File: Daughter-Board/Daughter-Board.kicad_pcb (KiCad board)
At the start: 2 copper layers, 79 parts, among them J201 302-S101, J301 Conn_01x08_0.5mm_Female_Kyoce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, J401 Conn_01x08_0.5mm_Female_Kyoce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, J501 Conn_01x08_0.5mm_Female_Kyoce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, J601 Conn_01x08_0.5mm_Female_Kyoce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, P101 EdgeConn, P102 EdgeConn, U101 LMV934MA, U102 MC74VHCT126A, U103 MC74VHCT126A, U104 4016, U105 4016, U106 4016, U107 4016, U108 4016, U201 74HC540, U202 PIC32MZ2048EFM064-TQFP, U301 LM324A

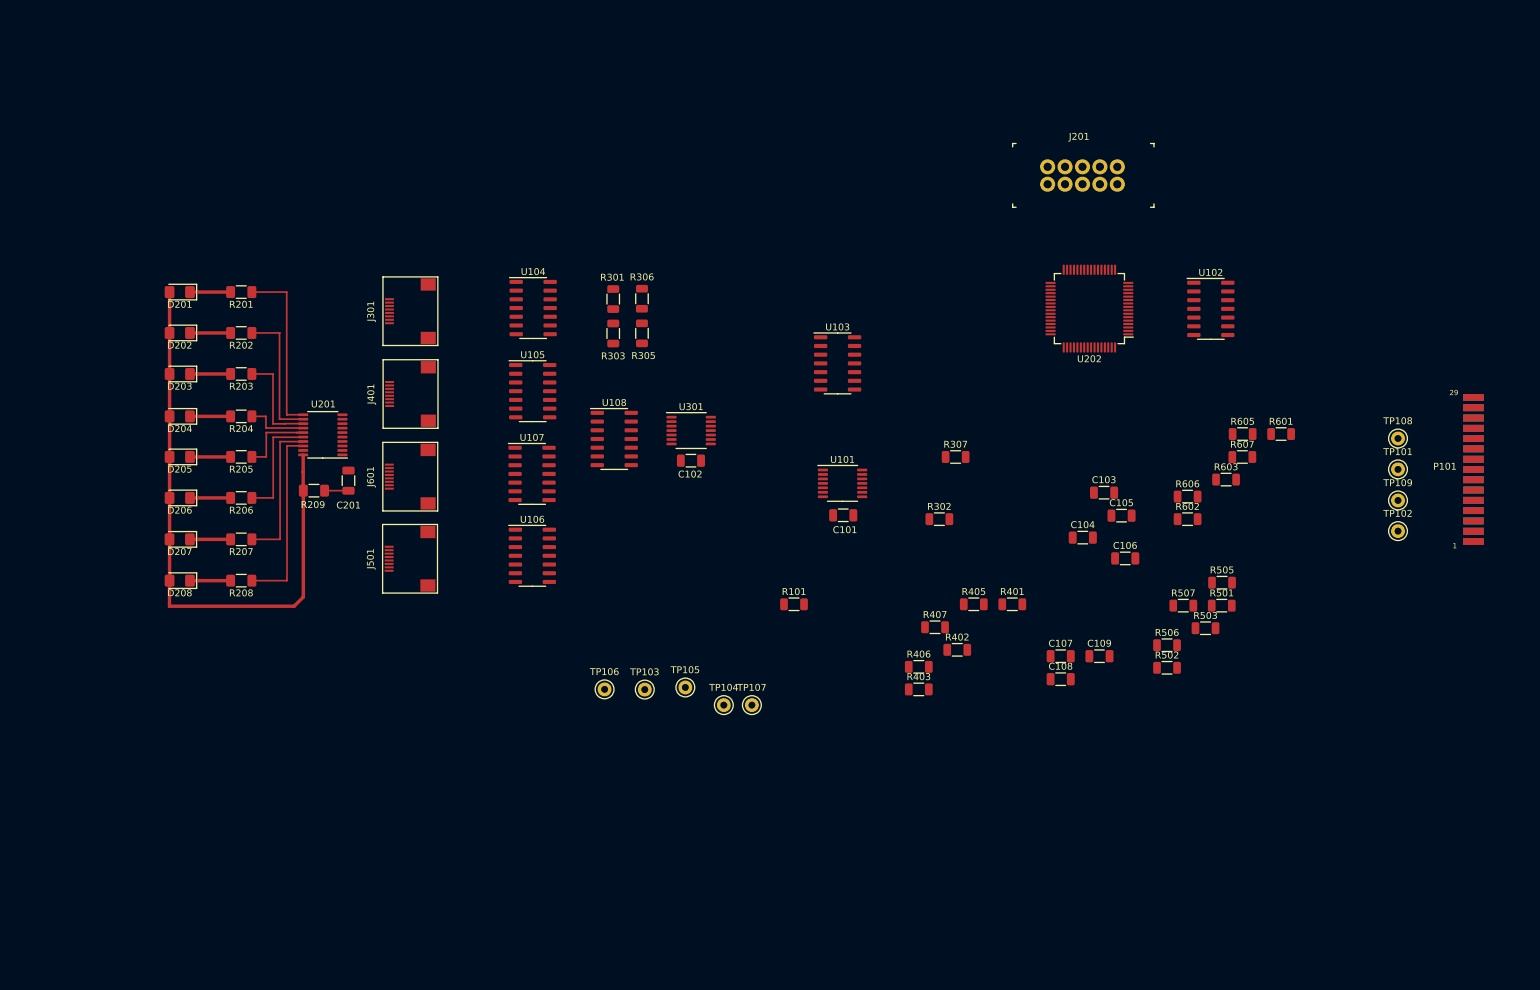
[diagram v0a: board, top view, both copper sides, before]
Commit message: Add test points to Digital and Daughter-Board schematics
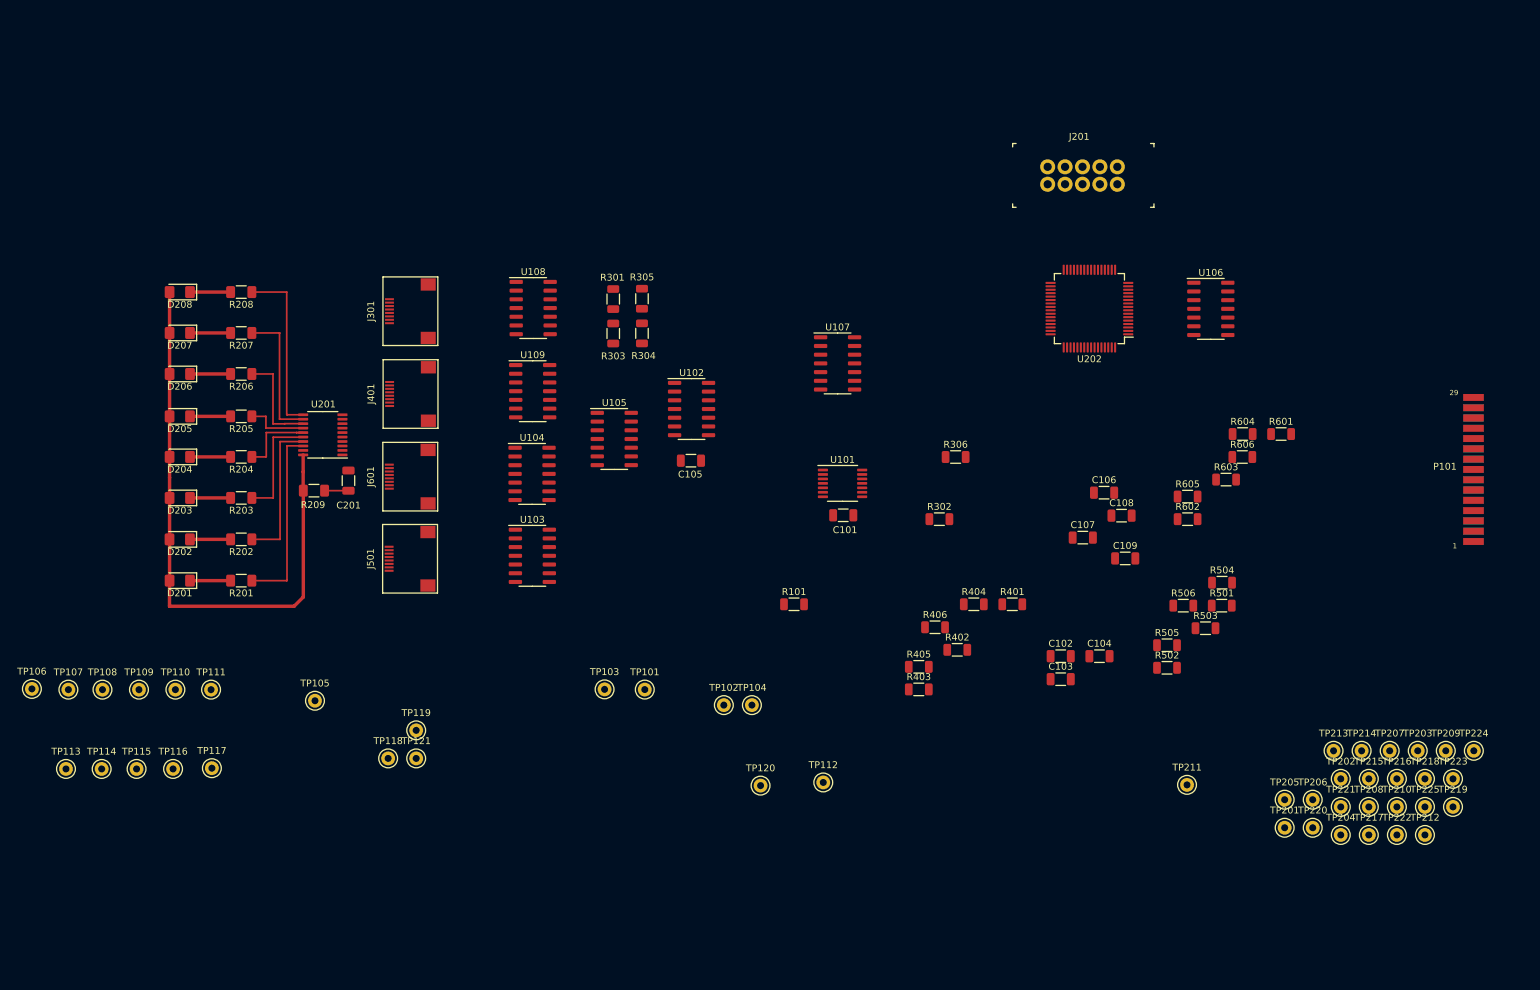
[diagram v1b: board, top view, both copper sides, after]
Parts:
- removed the TP101 at (74.0, -73.0)
- removed the TP102 at (74.0, -64.0)
- removed U301: LM324A, Package_SO:TSSOP-14_4.4x5mm_P0.65mm
- added TP106: 5000, digikey-footprints:Test_Point_D1.02mm, F.Cu at (-125.2, -41.0)
- added TP107: 5000, digikey-footprints:Test_Point_D1.02mm, F.Cu at (-119.8, -40.9)
- added TP110: 5000, digikey-footprints:Test_Point_D1.02mm, F.Cu at (-104.2, -40.9)
- added TP111: 5000, digikey-footprints:Test_Point_D1.02mm, F.Cu at (-99.0, -40.9)
- added TP112: 5000, digikey-footprints:Test_Point_D1.02mm, F.Cu at (-9.79, -27.4)
- added TP113: 5000, digikey-footprints:Test_Point_D1.02mm, F.Cu at (-120.2, -29.3)
- added TP114: 5000, digikey-footprints:Test_Point_D1.02mm, F.Cu at (-115.0, -29.3)
- added TP115: 5000, digikey-footprints:Test_Point_D1.02mm, F.Cu at (-109.9, -29.3)
- added TP116: 5000, digikey-footprints:Test_Point_D1.02mm, F.Cu at (-104.6, -29.3)
- added TP117: 5000, digikey-footprints:Test_Point_D1.02mm, F.Cu at (-98.9, -29.4)
- added TP118: 5000, digikey-footprints:Test_Point_D1.02mm, F.Cu at (-73.2, -30.9)
- added TP119: 5000, digikey-footprints:Test_Point_D1.02mm, F.Cu at (-69.1, -35.0)
- added TP120: 5000, digikey-footprints:Test_Point_D1.02mm, F.Cu at (-18.9, -26.9)
- added TP121: 5000, digikey-footprints:Test_Point_D1.02mm, F.Cu at (-69.1, -30.9)
- added TP201: 5000, digikey-footprints:Test_Point_D1.02mm, F.Cu at (57.5, -20.8)
- added TP202: 5000, digikey-footprints:Test_Point_D1.02mm, F.Cu at (65.7, -27.9)
- added TP203: 5000, digikey-footprints:Test_Point_D1.02mm, F.Cu at (76.9, -32.0)
- added TP204: 5000, digikey-footprints:Test_Point_D1.02mm, F.Cu at (65.7, -19.7)
- added TP205: 5000, digikey-footprints:Test_Point_D1.02mm, F.Cu at (57.5, -24.9)
- added TP206: 5000, digikey-footprints:Test_Point_D1.02mm, F.Cu at (61.6, -24.9)
- added TP207: 5000, digikey-footprints:Test_Point_D1.02mm, F.Cu at (72.8, -32.0)
- added TP208: 5000, digikey-footprints:Test_Point_D1.02mm, F.Cu at (69.7, -23.8)
- added TP209: 5000, digikey-footprints:Test_Point_D1.02mm, F.Cu at (81.0, -32.0)
- added TP210: 5000, digikey-footprints:Test_Point_D1.02mm, F.Cu at (73.8, -23.8)
- added TP211: 5000, digikey-footprints:Test_Point_D1.02mm, F.Cu at (43.2, -27.0)
- added TP212: 5000, digikey-footprints:Test_Point_D1.02mm, F.Cu at (77.9, -19.7)
- added TP213: 5000, digikey-footprints:Test_Point_D1.02mm, F.Cu at (64.6, -32.0)
- added TP214: 5000, digikey-footprints:Test_Point_D1.02mm, F.Cu at (68.7, -32.0)
- added TP215: 5000, digikey-footprints:Test_Point_D1.02mm, F.Cu at (69.7, -27.9)
- added TP216: 5000, digikey-footprints:Test_Point_D1.02mm, F.Cu at (73.8, -27.9)
- added TP217: 5000, digikey-footprints:Test_Point_D1.02mm, F.Cu at (69.7, -19.7)
- added TP218: 5000, digikey-footprints:Test_Point_D1.02mm, F.Cu at (77.9, -27.9)
- added TP219: 5000, digikey-footprints:Test_Point_D1.02mm, F.Cu at (82.0, -23.8)
- added TP220: 5000, digikey-footprints:Test_Point_D1.02mm, F.Cu at (61.6, -20.8)
- added TP221: 5000, digikey-footprints:Test_Point_D1.02mm, F.Cu at (65.7, -23.8)
- added TP222: 5000, digikey-footprints:Test_Point_D1.02mm, F.Cu at (73.8, -19.7)
- added TP223: 5000, digikey-footprints:Test_Point_D1.02mm, F.Cu at (82.0, -27.9)
- added TP224: 5000, digikey-footprints:Test_Point_D1.02mm, F.Cu at (85.1, -32.0)
- added TP225: 5000, digikey-footprints:Test_Point_D1.02mm, F.Cu at (77.9, -23.8)
- added U102: LM324A, Package_SO:SOIC-14_3.9x8.7mm_P1.27mm, F.Cu at (-29.0, -81.8)
- moved TP108 192.4 mm to (-114.9, -40.9)
- moved TP109 185.6 mm to (-109.5, -40.9)
- moved TP105 54.0 mm to (-83.9, -39.3)
- renumbered C107 to C102, C108 to C103, C109 to C104, C102 to C105, C103 to C106, C104 to C107, C105 to C108, C106 to C109, D208 to D201, D207 to D202, D206 to D203, D205 to D204, D204 to D205, D203 to D206, D202 to D207, D201 to D208, R208 to R201, R207 to R202, R206 to R203, R205 to R204, R204 to R205, R203 to R206, R202 to R207, R201 to R208, R305 to R304, R306 to R305, R307 to R306, R405 to R404, R406 to R405, R407 to R406, R505 to R504, R506 to R505, R507 to R506, R605 to R604, R606 to R605, R607 to R606, TP103 to TP101, TP104 to TP102, TP106 to TP103, TP107 to TP104, U106 to U103, U107 to U104, U108 to U105, U102 to U106, U103 to U107, U104 to U108, U105 to U109
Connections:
- J301 pad 7: /Digital/Word_Select -> /Digital/Word_Strobe
- J401 pad 7: /Digital/Word_Select -> /Digital/Word_Strobe
- J501 pad 7: /Digital/Word_Select -> /Digital/Word_Strobe
- J601 pad 7: /Digital/Word_Select -> /Digital/Word_Strobe
- TP105 pad 1: /Digital/CLK_EN -> /Mic_Interface_2/V_Bias
- TP108 pad 1: /Data_Out -> GNDREF
- TP109 pad 1: /MB_Comm_En -> GNDREF
- U202 pad 18: /Digital/Word_Select -> /Digital/Word_Strobe
- U202 pad 30: /Digital/DOut_EN_4 -> /Digital/Word_Strobe
- U202 pad 43: /Digital/DOut_EN_4 -> /Digital/Word_Strobe

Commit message: Update component footprint for U102E.
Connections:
- U103 pad 10: Net-(R504-Pad2) -> /Digital/DOut
- U103 pad 11: /Mic_Interface_4/AOut -> Net-(J501-Pad4)
- U103 pad 12: /Digital/No_Gain -> /Digital/DOut_EN_4
- U104 pad 10: Net-(R604-Pad2) -> /Digital/DOut
- U104 pad 11: /Mic_Interface_3/AOut -> Net-(J601-Pad4)
- U104 pad 12: /Digital/No_Gain -> /Digital/DOut_EN_3
- U105 pad 1: Net-(J301-Pad4) -> /Mic_Interface_1/AOut
- U105 pad 10: /Digital/DOut -> Net-(R604-Pad2)
- U105 pad 11: Net-(J601-Pad4) -> /Mic_Interface_3/AOut
- U105 pad 12: /Digital/DOut_EN_3 -> /Digital/No_Gain
- U105 pad 13: /Digital/DOut_EN_1 -> /Digital/No_Gain
- U105 pad 2: /Digital/DOut -> Net-(R304-Pad2)
- U105 pad 3: /Digital/DOut -> Net-(R404-Pad2)
- U105 pad 4: Net-(J401-Pad4) -> /Mic_Interface_2/AOut
- U105 pad 5: /Digital/DOut_EN_2 -> /Digital/No_Gain
- U105 pad 6: /Digital/DOut_EN_4 -> /Digital/No_Gain
- U105 pad 8: Net-(J501-Pad4) -> /Mic_Interface_4/AOut
- U105 pad 9: /Digital/DOut -> Net-(R504-Pad2)
- U108 pad 10: Net-(R304-Pad2) -> /Digital/DOut
- U108 pad 11: /Mic_Interface_1/AOut -> Net-(J301-Pad4)
- U108 pad 12: /Digital/No_Gain -> /Digital/DOut_EN_1
- U109 pad 10: Net-(R404-Pad2) -> /Digital/DOut
- U109 pad 11: /Mic_Interface_2/AOut -> Net-(J401-Pad4)
- U109 pad 12: /Digital/No_Gain -> /Digital/DOut_EN_2
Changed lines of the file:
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@@
       (net 103 "Net-(R304-Pad1)"))
     (pad 10 smd roundrect (at 2.475 1.27) (size 1.95 0.6) (layers F.Cu F.Paste F.Mask) (roundrect_rratio 0.25)
-      (net 104 "Net-(R304-Pad2)"))
+      (net 35 /Digital/DOut))
     (pad 11 smd roundrect (at 2.475 0) (size 1.95 0.6) (layers F.Cu F.Paste F.Mask) (roundrect_rratio 0.25)
-      (net 41 /Mic_Interface_1/AOut))
+      (net 12 "Net-(J301-Pad4)"))
     (pad 12 smd roundrect (at 2.475 -1.27) (size 1.95 0.6) (layers F.Cu F.Paste F.Mask) (roundrect_rratio 0.25)
-      (net 40 /Digital/No_Gain))
+      (net 36 /Digital/DOut_EN_1))
     (pad 13 smd roundrect (at 2.475 -2.54) (size 1.95 0.6) (layers F.Cu F.Paste F.Mask) (roundrect_rratio 0.25)
       (net 37 /Digital/PlusEn))
@@
       (net 37 /Digital/PlusEn))
     (pad 12 smd roundrect (at 2.475 -1.27) (size 1.95 0.6) (layers F.Cu F.Paste F.Mask) (roundrect_rratio 0.25)
-      (net 40 /Digital/No_Gain))
+      (net 42 /Digital/DOut_EN_2))
     (pad 11 smd roundrect (at 2.475 0) (size 1.95 0.6) (layers F.Cu F.Paste F.Mask) (roundrect_rratio 0.25)
-      (net 44 /Mic_Interface_2/AOut))
+      (net 18 "Net-(J401-Pad4)"))
     (pad 10 smd roundrect (at 2.475 1.27) (size 1.95 0.6) (layers F.Cu F.Paste F.Mask) (roundrect_rratio 0.25)
-      (net 105 "Net-(R404-Pad2)"))
+      (net 35 /Digital/DOut))
     (pad 9 smd roundrect (at 2.475 2.54) (size 1.95 0.6) (layers F.Cu F.Paste F.Mask) (roundrect_rratio 0.25)
       (net 106 "Net-(R404-Pad1)"))
@@
       (net 108 "Net-(R504-Pad1)"))
     (pad 10 smd roundrect (at 2.475 1.27) (size 1.95 0.6) (layers F.Cu F.Paste F.Mask) (roundrect_rratio 0.25)
-      (net 107 "Net-(R504-Pad2)"))
+      (net 35 /Digital/DOut))
     (pad 11 smd roundrect (at 2.475 0) (size 1.95 0.6) (layers F.Cu F.Paste F.Mask) (roundrect_rratio 0.25)
-      (net 47 /Mic_Interface_4/AOut))
+      (net 23 "Net-(J501-Pad4)"))
     (pad 12 smd roundrect (at 2.475 -1.27) (size 1.95 0.6) (layers F.Cu F.Paste F.Mask) (roundrect_rratio 0.25)
-      (net 40 /Digital/No_Gain))
+      (net 45 /Digital/DOut_EN_4))
     (pad 13 smd roundrect (at 2.475 -2.54) (size 1.95 0.6) (layers F.Cu F.Paste F.Mask) (roundrect_rratio 0.25)
       (net 46 /Mic_Interface_4/PlusEn))
@@
       (net 37 /Digital/PlusEn))
     (pad 12 smd roundrect (at 2.475 -1.27) (size 1.95 0.6) (layers F.Cu F.Paste F.Mask) (roundrect_rratio 0.25)
-      (net 40 /Digital/No_Gain))
+      (net 48 /Digital/DOut_EN_3))
     (pad 11 smd roundrect (at 2.475 0) (size 1.95 0.6) (layers F.Cu F.Paste F.Mask) (roundrect_rratio 0.25)
-      (net 49 /Mic_Interface_3/AOut))
+      (net 28 "Net-(J601-Pad4)"))
     (pad 10 smd roundrect (at 2.475 1.27) (size 1.95 0.6) (layers F.Cu F.Paste F.Mask) (roundrect_rratio 0.25)
-      (net 110 "Net-(R604-Pad2)"))
+      (net 35 /Digital/DOut))
     (pad 9 smd roundrect (at 2.475 2.54) (size 1.95 0.6) (layers F.Cu F.Paste F.Mask) (roundrect_rratio 0.25)
       (net 109 "Net-(R604-Pad1)"))
@@
     )
     (pad 1 smd roundrect (at -2.475 -3.81) (size 1.95 0.6) (layers F.Cu F.Paste F.Mask) (roundrect_rratio 0.25)
-      (net 12 "Net-(J301-Pad4)"))
+      (net 41 /Mic_Interface_1/AOut))
     (pad 2 smd roundrect (at -2.475 -2.54) (size 1.95 0.6) (layers F.Cu F.Paste F.Mask) (roundrect_rratio 0.25)
-      (net 35 /Digital/DOut))
+      (net 104 "Net-(R304-Pad2)"))
     (pad 3 smd roundrect (at -2.475 -1.27) (size 1.95 0.6) (layers F.Cu F.Paste F.Mask) (roundrect_rratio 0.25)
-      (net 35 /Digital/DOut))
+      (net 105 "Net-(R404-Pad2)"))
     (pad 4 smd roundrect (at -2.475 0) (size 1.95 0.6) (layers F.Cu F.Paste F.Mask) (roundrect_rratio 0.25)
-      (net 18 "Net-(J401-Pad4)"))
+      (net 44 /Mic_Interface_2/AOut))
     (pad 5 smd roundrect (at -2.475 1.27) (size 1.95 0.6) (layers F.Cu F.Paste F.Mask) (roundrect_rratio 0.25)
-      (net 42 /Digital/DOut_EN_2))
+      (net 40 /Digital/No_Gain))
     (pad 6 smd roundrect (at -2.475 2.54) (size 1.95 0.6) (layers F.Cu F.Paste F.Mask) (roundrect_rratio 0.25)
-      (net 45 /Digital/DOut_EN_4))
+      (net 40 /Digital/No_Gain))
     (pad 7 smd roundrect (at -2.475 3.81) (size 1.95 0.6) (layers F.Cu F.Paste F.Mask) (roundrect_rratio 0.25)
       (net 2 GNDREF))
     (pad 8 smd roundrect (at 2.475 3.81) (size 1.95 0.6) (layers F.Cu F.Paste F.Mask) (roundrect_rratio 0.25)
-      (net 23 "Net-(J501-Pad4)"))
+      (net 47 /Mic_Interface_4/AOut))
     (pad 9 smd roundrect (at 2.475 2.54) (size 1.95 0.6) (layers F.Cu F.Paste F.Mask) (roundrect_rratio 0.25)
-      (net 35 /Digital/DOut))
+      (net 107 "Net-(R504-Pad2)"))
     (pad 10 smd roundrect (at 2.475 1.27) (size 1.95 0.6) (layers F.Cu F.Paste F.Mask) (roundrect_rratio 0.25)
-      (net 35 /Digital/DOut))
+      (net 110 "Net-(R604-Pad2)"))
     (pad 11 smd roundrect (at 2.475 0) (size 1.95 0.6) (layers F.Cu F.Paste F.Mask) (roundrect_rratio 0.25)
-      (net 28 "Net-(J601-Pad4)"))
+      (net 49 /Mic_Interface_3/AOut))
     (pad 12 smd roundrect (at 2.475 -1.27) (size 1.95 0.6) (layers F.Cu F.Paste F.Mask) (roundrect_rratio 0.25)
-      (net 48 /Digital/DOut_EN_3))
+      (net 40 /Digital/No_Gain))
     (pad 13 smd roundrect (at 2.475 -2.54) (size 1.95 0.6) (layers F.Cu F.Paste F.Mask) (roundrect_rratio 0.25)
-      (net 36 /Digital/DOut_EN_1))
+      (net 40 /Digital/No_Gain))
     (pad 14 smd roundrect (at 2.475 -3.81) (size 1.95 0.6) (layers F.Cu F.Paste F.Mask) (roundrect_rratio 0.25)
       (net 1 +5V))

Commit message: Corrected analog gain switch position.
Analog gain switch was across the feedback resistor. It is changed to grounding of the - input resistor to the op amp.
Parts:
- moved U105 35.9 mm to (-4.57, -81.1)
- moved U107 20.8 mm to (-8.12, -109.2)
- moved U106 16.3 mm to (57.4, -108.7)
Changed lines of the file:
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@@
   )
   (module Package_SO:SOIC-14_3.9x8.7mm_P1.27mm (layer F.Cu)
-    (at 46.71 -96.41)
+    (at 57.41 -108.67)
     (descr "SOIC, 14 Pin (JEDEC MS-012AB, https://www.analog.com/media/en/package-pcb-resources/package/pkg_pdf/soic_narrow-r/r_14.pdf), generated with kicad-footprint-generator ipc_gullwing_generator.py")
     (tags "SOIC SO")
@@
   )
   (module Package_SO:SOIC-14_3.9x8.7mm_P1.27mm (layer F.Cu)
-    (at -7.7 -88.46)
+    (at -8.12 -109.25)
     (descr "SOIC, 14 Pin (JEDEC MS-012AB, https://www.analog.com/media/en/package-pcb-resources/package/pkg_pdf/soic_narrow-r/r_14.pdf), generated with kicad-footprint-generator ipc_gullwing_generator.py")
     (tags "SOIC SO")
@@
   )
   (module Package_SO:SOIC-14_3.9x8.7mm_P1.27mm (layer F.Cu)
-    (at -40.26 -77.44)
+    (at -4.57 -81.12)
     (descr "SOIC, 14 Pin (JEDEC MS-012AB, https://www.analog.com/media/en/package-pcb-resources/package/pkg_pdf/soic_narrow-r/r_14.pdf), generated with kicad-footprint-generator ipc_gullwing_generator.py")
     (tags "SOIC SO")
